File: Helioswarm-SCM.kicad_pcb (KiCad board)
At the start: 8 copper layers, 38 parts, among them U201 ASIC_JUICE

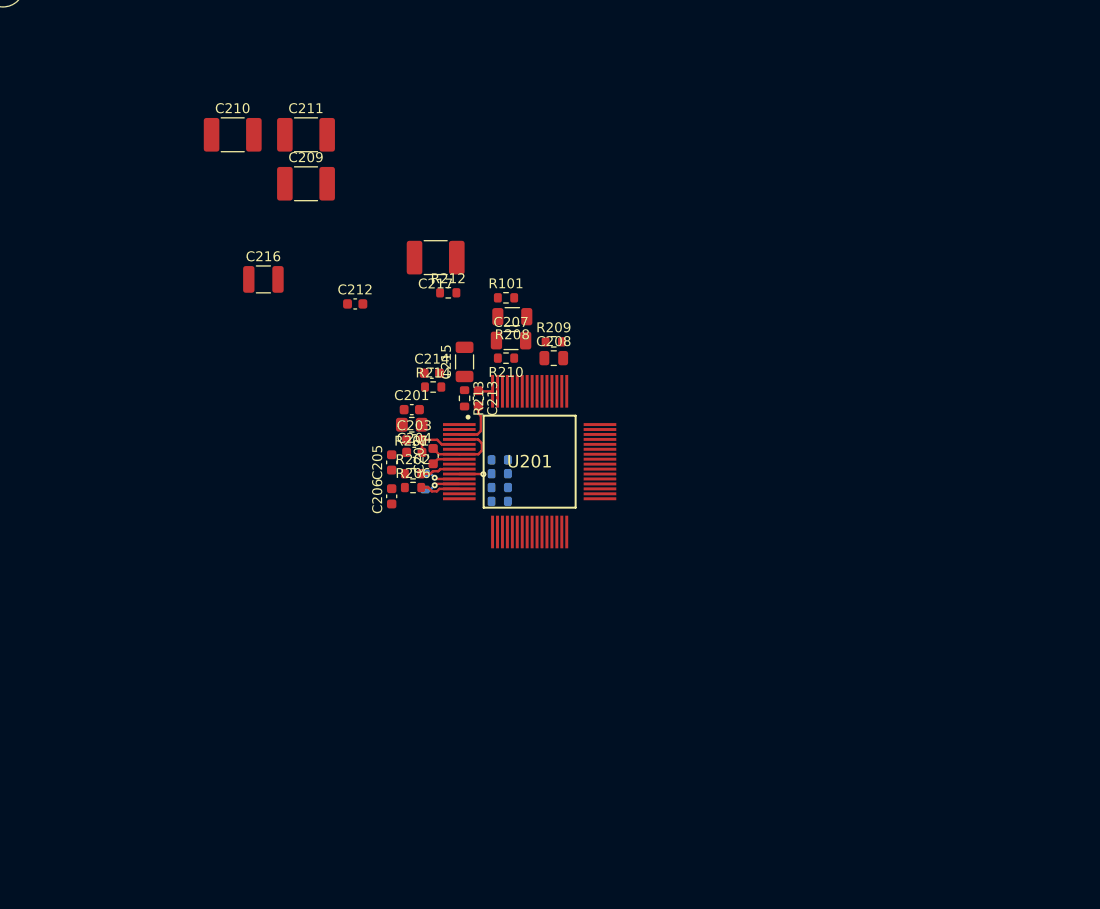
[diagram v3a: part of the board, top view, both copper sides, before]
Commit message: Layout WIP
Asic mostly routed, D-Sub connectors layout started.

Signed-off-by: Alexis Jeandet <alexis.jeandet@member.fsf.org>
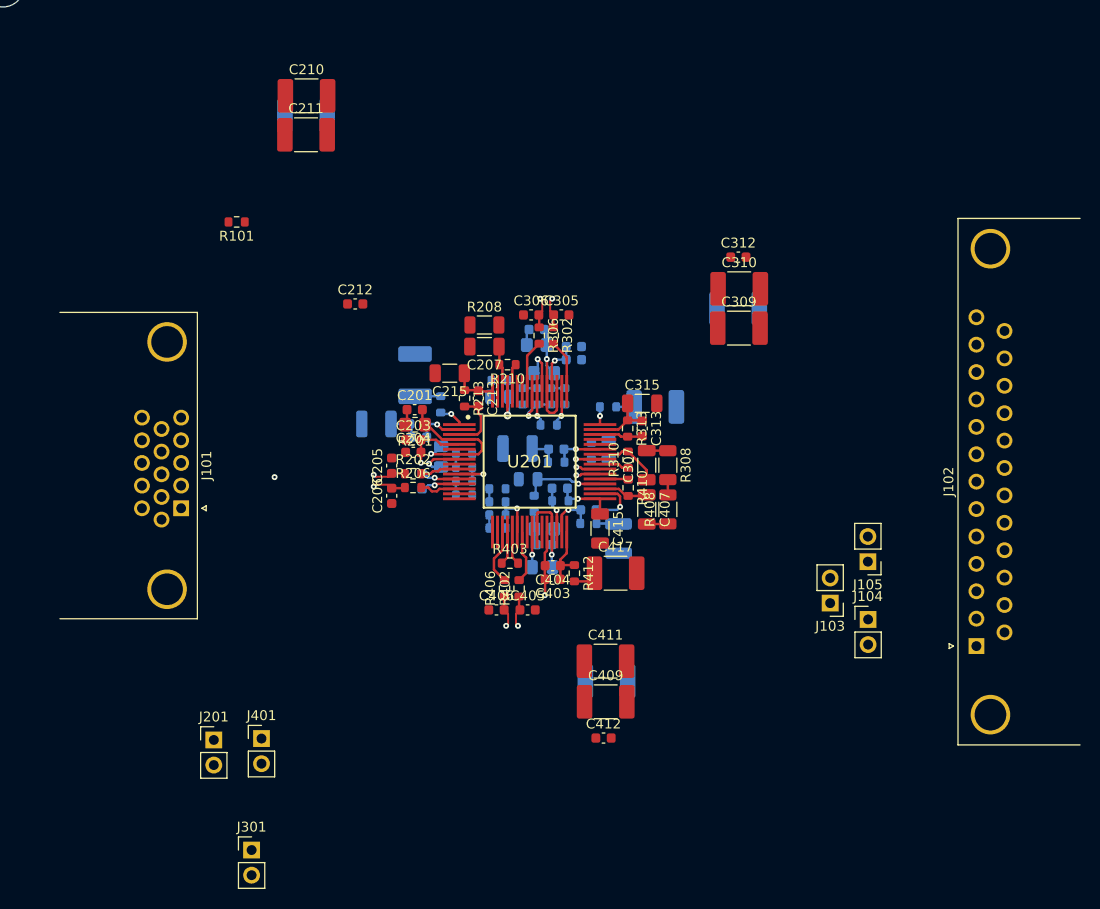
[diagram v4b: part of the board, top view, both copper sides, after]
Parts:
- added C301: *, Capacitor_SMD:C_0603_1608Metric, B.Cu at (156.3, 73.6)
- added C302: *, Capacitor_SMD:C_0805_2012Metric_Pad1.18x1.45mm_HandSolder, B.Cu at (157.0, 78.0)
- added C303: *, Capacitor_SMD:C_0603_1608Metric, B.Cu at (160.0, 76.6)
- added C304: *, Capacitor_SMD:C_0603_1608Metric, B.Cu at (160.0, 75.3)
- added C305: *, Capacitor_SMD:C_0603_1608Metric, F.Cu at (158.8, 72.1)
- added C306: *, Capacitor_SMD:C_0603_1608Metric, F.Cu at (155.7, 72.1)
- added C307: 220n, Capacitor_SMD:C_1206_3216Metric, F.Cu at (167.4, 87.3)
- added C308: *, Capacitor_SMD:C_0805_2012Metric, B.Cu at (163.5, 85.7)
- added C309: 680n, Capacitor_SMD:C_1812_4532Metric_Pad1.57x3.40mm_HandSolder, F.Cu at (176.7, 73.4)
- added C310: 680n, Capacitor_SMD:C_1812_4532Metric_Pad1.57x3.40mm_HandSolder, F.Cu at (176.7, 69.4)
- added C311: 680n, Capacitor_SMD:C_1812_4532Metric_Pad1.57x3.40mm_HandSolder, B.Cu at (176.6, 71.4)
- added C312: 1n, Capacitor_SMD:C_0603_1608Metric, F.Cu at (176.6, 66.2)
- added C313: 221p, Capacitor_SMD:C_0603_1608Metric, F.Cu at (166.9, 83.6)
- added C314: 221p, Capacitor_SMD:C_0603_1608Metric, B.Cu at (158.2, 85.6)
- added C315: 220n, Capacitor_SMD:C_1206_3216Metric, F.Cu at (166.9, 81.0)
- added C316: 470nF, Capacitor_SMD:C_1210_3225Metric, B.Cu at (154.3, 85.6)
- added C317: 470n, Capacitor_SMD:C_1812_4532Metric_Pad1.57x3.40mm_HandSolder, B.Cu at (168.2, 81.4)
- added C401: *, Capacitor_SMD:C_0603_1608Metric, B.Cu at (157.0, 95.3)
- added C402: *, Capacitor_SMD:C_0805_2012Metric_Pad1.18x1.45mm_HandSolder, B.Cu at (156.8, 97.6)
- added C403: *, Capacitor_SMD:C_0603_1608Metric, F.Cu at (157.9, 98.8)
- added C404: *, Capacitor_SMD:C_0603_1608Metric, F.Cu at (157.9, 97.4)
- added C405: *, Capacitor_SMD:C_0603_1608Metric, F.Cu at (155.3, 101.9)
- added C406: *, Capacitor_SMD:C_0603_1608Metric, F.Cu at (152.2, 101.9)
- added C407: 220n, Capacitor_SMD:C_1206_3216Metric, F.Cu at (167.4, 91.7)
- added C408: *, Capacitor_SMD:C_0805_2012Metric, B.Cu at (155.4, 88.7)
- added C409: 680n, Capacitor_SMD:C_1812_4532Metric_Pad1.57x3.40mm_HandSolder, F.Cu at (163.2, 111.2)
- added C410: 680n, Capacitor_SMD:C_1812_4532Metric_Pad1.57x3.40mm_HandSolder, B.Cu at (163.3, 109.1)
- added C411: 680n, Capacitor_SMD:C_1812_4532Metric_Pad1.57x3.40mm_HandSolder, F.Cu at (163.2, 107.1)
- added C412: 1n, Capacitor_SMD:C_0603_1608Metric, F.Cu at (163.0, 114.9)
- added C413: 221p, Capacitor_SMD:C_0603_1608Metric, B.Cu at (158.6, 89.6)
- added C414: 221p, Capacitor_SMD:C_0603_1608Metric, B.Cu at (161.5, 91.8)
- added C415: 220n, Capacitor_SMD:C_1206_3216Metric, F.Cu at (162.7, 93.7)
- added C416: 470nF, Capacitor_SMD:C_1210_3225Metric, B.Cu at (164.5, 94.7)
- added C417: 470n, Capacitor_SMD:C_1812_4532Metric_Pad1.57x3.40mm_HandSolder, F.Cu at (164.2, 98.2)
- added J101: DB15_Male_MountingHoles, Connector_Dsub:DSUB-15-HD_Female_Horizontal_P2.29x1.98mm_EdgePinOffset8.35mm_Housed_MountingHolesOffset10.89mm, F.Cu at (120.3, 91.6)
- added J102: DB25_Female_MountingHoles, Connector_Dsub:DSUB-25_Male_Horizontal_P2.77x2.84mm_EdgePinOffset7.70mm_Housed_MountingHolesOffset9.12mm, F.Cu at (200.7, 105.6)
- added J103: Conn_01x02, Connector_PinHeader_2.54mm:PinHeader_1x02_P2.54mm_Vertical, F.Cu at (185.9, 101.2)
- added J104: Conn_01x02, Connector_PinHeader_2.54mm:PinHeader_1x02_P2.54mm_Vertical, F.Cu at (189.8, 102.9)
- added J105: Conn_01x02, Connector_PinHeader_2.54mm:PinHeader_1x02_P2.54mm_Vertical, F.Cu at (189.7, 97.0)
- added J201: Conn_01x02, Connector_PinHeader_2.54mm:PinHeader_1x02_P2.54mm_Vertical, F.Cu at (123.6, 115.0)
- added J301: Conn_01x02, Connector_PinHeader_2.54mm:PinHeader_1x02_P2.54mm_Vertical, F.Cu at (127.4, 126.2)
- added J401: Conn_01x02, Connector_PinHeader_2.54mm:PinHeader_1x02_P2.54mm_Vertical, F.Cu at (128.4, 114.9)
- added R301: 150k, Resistor_SMD:R_0805_2012Metric_Pad1.20x1.40mm_HandSolder, B.Cu at (156.3, 75.1)
- added R302: 49,9, Resistor_SMD:R_0603_1608Metric, F.Cu at (157.9, 74.2)
- added R303: 7,68k, Resistor_SMD:R_0603_1608Metric, B.Cu at (157.5, 83.2)
- added R304: 49,9k, Resistor_SMD:R_0603_1608Metric, B.Cu at (159.1, 80.3)
- added R305: TBD, Resistor_SMD:R_0603_1608Metric, B.Cu at (157.7, 80.3)
- added R306: 49,9, Resistor_SMD:R_0603_1608Metric, F.Cu at (156.5, 74.2)
- added R307: TBD, Resistor_SMD:R_0603_1608Metric, B.Cu at (156.3, 80.3)
- added R308: 750k, Resistor_SMD:R_1206_3216Metric, F.Cu at (169.5, 87.3)
- added R309: 42,2k, Resistor_SMD:R_0603_1608Metric, B.Cu at (161.8, 85.9)
- added R310: 24,9k, Resistor_SMD:R_0603_1608Metric, F.Cu at (165.5, 86.7)
- added R311: 49,9k, Resistor_SMD:R_0603_1608Metric, B.Cu at (154.8, 80.3)
- added R312: 400, Resistor_SMD:R_0603_1608Metric, B.Cu at (163.5, 81.4)
- added R313: 22,1k, Resistor_SMD:R_0603_1608Metric, F.Cu at (165.5, 83.6)
- added R314: 44,2k, Resistor_SMD:R_0603_1608Metric, B.Cu at (158.2, 87.0)
- added R401: 150k, Resistor_SMD:R_0805_2012Metric_Pad1.20x1.40mm_HandSolder, B.Cu at (157.0, 93.7)
- added R402: 49,9, Resistor_SMD:R_0603_1608Metric, F.Cu at (154.5, 99.7)
- added R403: 7,68k, Resistor_SMD:R_0603_1608Metric, F.Cu at (153.6, 97.2)
- added R404: 49,9k, Resistor_SMD:R_0603_1608Metric, B.Cu at (152.3, 93.6)
- added R405: TBD, Resistor_SMD:R_0603_1608Metric, B.Cu at (152.3, 92.3)
- added R406: 49,9, Resistor_SMD:R_0603_1608Metric, F.Cu at (153.0, 99.7)
- added R407: TBD, Resistor_SMD:R_0603_1608Metric, B.Cu at (152.3, 91.0)
- added R408: 750k, Resistor_SMD:R_1206_3216Metric, F.Cu at (169.5, 91.7)
- added R409: 42,2k, Resistor_SMD:R_0603_1608Metric, B.Cu at (156.0, 91.2)
- added R410: 24,9k, Resistor_SMD:R_0603_1608Metric, F.Cu at (165.5, 89.6)
- added R411: 49,9k, Resistor_SMD:R_0603_1608Metric, B.Cu at (152.3, 89.7)
- added R412: 400, Resistor_SMD:R_0603_1608Metric, F.Cu at (160.1, 98.2)
- added R413: 22,1k, Resistor_SMD:R_0603_1608Metric, B.Cu at (158.6, 90.9)
- added R414: 44,2k, Resistor_SMD:R_0603_1608Metric, B.Cu at (161.5, 93.2)
- C202: footprint Capacitor_SMD:C_0603_1608Metric -> Capacitor_SMD:C_0805_2012Metric_Pad1.18x1.45mm_HandSolder; moved to B.Cu
- C208, C209, C214, C216, C217, R209, R212, R214: moved to B.Cu
- moved R101 28.3 mm to (125.9, 62.7), turned to 180 degrees
- moved C216 18.5 mm to (140.1, 83.1), turned to 180 degrees
- moved C217 12.1 mm to (144.0, 78.2), turned to 90 degrees
- moved R212 11.3 mm to (146.6, 81.1), turned to 90 degrees
- moved C210 8.44 mm to (133.0, 49.9)
- moved C209 6.91 mm to (132.9, 51.9)
- moved C208 6.74 mm to (152.5, 80.4), turned to 180 degrees
- moved R209 6.74 mm to (152.5, 78.7), turned to 180 degrees
- moved C214 6.58 mm to (144.4, 84.4)
- moved R211 6.02 mm to (148.9, 86.1), turned to 0 degrees
- moved R204 5.06 mm to (148.9, 90.3), turned to 0 degrees
- moved R207 4.14 mm to (148.9, 87.5), turned to 180 degrees
- moved R214 4.01 mm to (144.3, 83.1)
- moved R205 3.69 mm to (148.9, 88.9), turned to 180 degrees
- moved R208 2.94 mm to (151.0, 73.1), turned to 0 degrees
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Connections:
- C201 pad 1: /ASIC_X_Channel/CR -> /CR_X
- R201 pad 2: /ASIC_X_Channel/CR -> /CR_X
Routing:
- net /SX-: track 0.00 -> 76.5 mm, vias 0 -> 1
- net /SX+: track 0.00 -> 76.4 mm, vias 0 -> 1
- net /SY-: track 0.00 -> 71.0 mm, vias 0 -> 1
- net /SY+: track 0.00 -> 69.8 mm, vias 0 -> 1
- net /SZ-: track 0.00 -> 56.3 mm, vias 0 -> 1
- net /SZ+: track 0.00 -> 55.1 mm, vias 0 -> 1
- net /SCM_Z: track 0.00 -> 50.7 mm, vias 0 -> 2
- net /SCM_Y: track 0.00 -> 47.8 mm, vias 0 -> 1
- net /SCM_X: track 5.23 -> 32.4 mm, vias 0 -> 1
- net /ASIC_Y_Channel/In2P: track 0.00 -> 13.1 mm, vias 0 -> 1
- net /ASIC_Z_Channel/In2P: track 0.00 -> 11.6 mm, vias 0 -> 1
- net /ASIC_Z_Channel/VDD: track 0.00 -> 9.39 mm, vias 0 -> 1
- net Net-(C408-Pad1): track 0.00 -> 8.31 mm, vias 0 -> 1
- net /ASIC_X_Channel/In2P: track 8.51 -> 15.9 mm, vias 0 -> 1
- net Net-(C307-Pad1): track 0.00 -> 6.60 mm
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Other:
- copper layers 8 -> 4

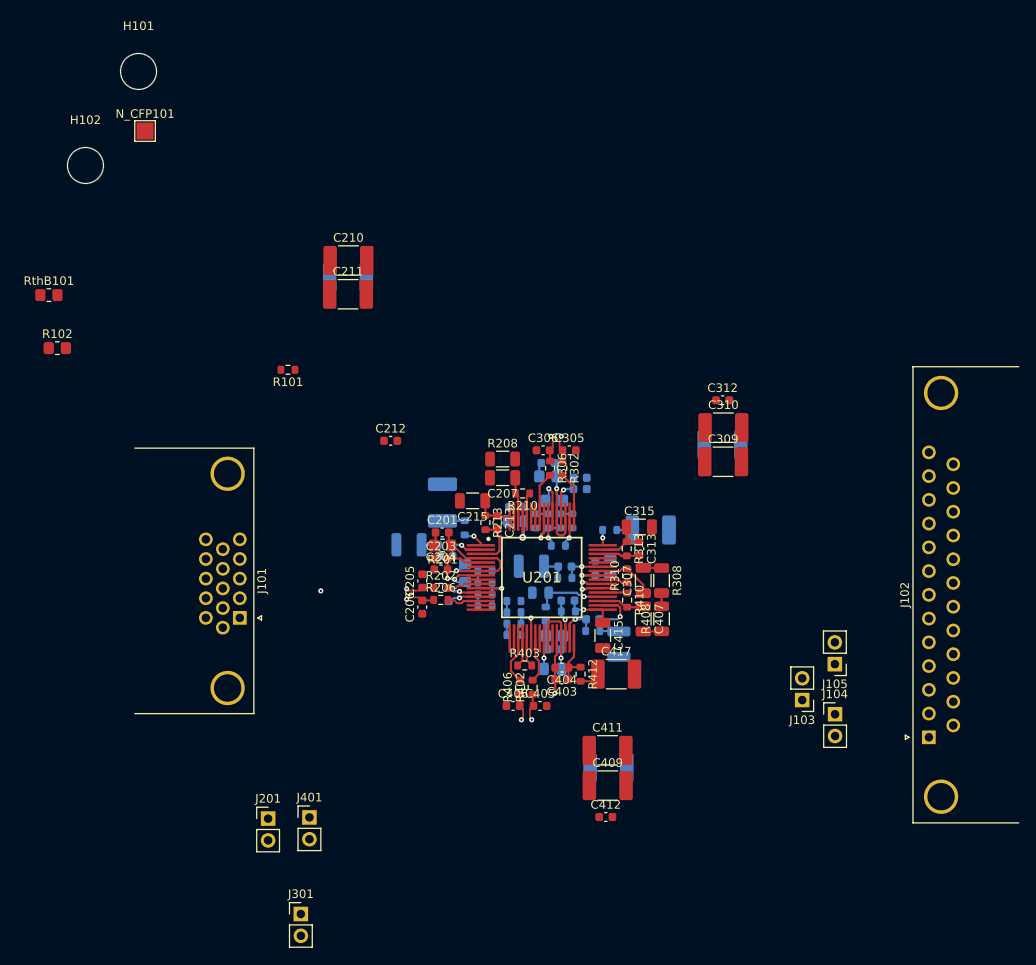
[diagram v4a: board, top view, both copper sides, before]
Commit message: PCB layout complete without silkscreen
Signed-off-by: Alexis Jeandet <alexis.jeandet@member.fsf.org>
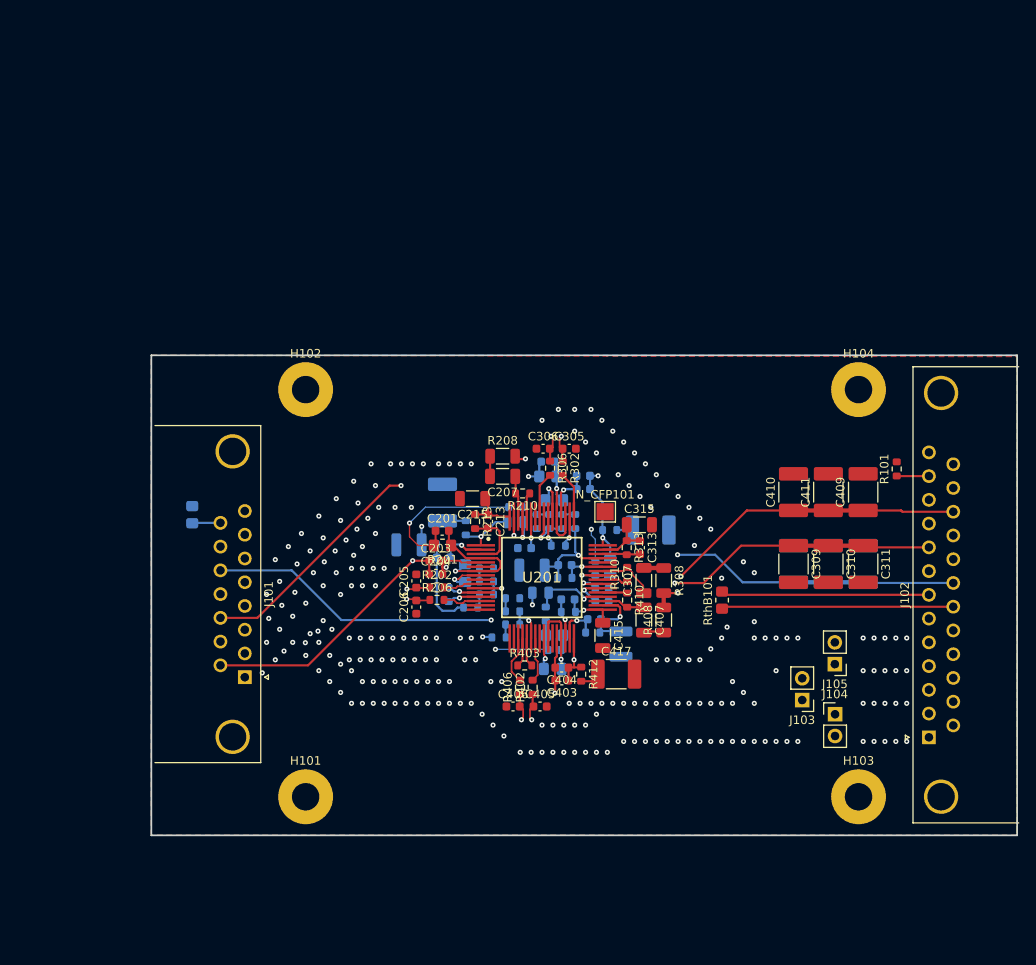
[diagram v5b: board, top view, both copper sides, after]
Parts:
- removed J201, J301, J401: Conn_01x02, Connector_PinHeader_2.54mm:PinHeader_1x02_P2.54mm_Vertical
- added H103: MountingHole_Pad, MountingHole:MountingHole_3.2mm_M3_Pad, F.Cu at (192.5, 112.5)
- added H104: MountingHole_Pad, MountingHole:MountingHole_3.2mm_M3_Pad, F.Cu at (192.5, 65.0)
- C210, C211, C212, C312, C412, R102: moved to B.Cu
- C311, C410: moved to F.Cu
- H101, H102: value MountingHole -> MountingHole_Pad; footprint LibPersoNadj:MountingHole_4.2 -> MountingHole:MountingHole_3.2mm_M3_Pad
- J101: value DB15_Male_MountingHoles -> DB15_Female_MountingHoles; footprint Connector_Dsub:DSUB-15-HD_Female_Horizontal_P2.29x1.98mm_EdgePinOffset8.35mm_Housed_MountingHolesOffset10.89mm -> Connector_Dsub:DSUB-15_Female_Horizontal_P2.77x2.84mm_EdgePinOffset7.70mm_Housed_MountingHolesOffset9.12mm
- moved H101 86.8 mm to (128.0, 112.5)
- moved RthB101 86.2 mm to (176.6, 89.6), turned to 90 degrees
- moved R101 72.0 mm to (197.0, 74.3), turned to 90 degrees
- moved C210 69.7 mm to (193.0, 85.3), turned to 90 degrees
- moved N_CFP101 69.7 mm to (162.9, 79.2)
- moved C211 64.3 mm to (189.0, 85.3), turned to 90 degrees
- moved C209 61.8 mm to (184.9, 85.3), turned to 90 degrees
- moved C409 45.4 mm to (193.0, 77.0), turned to 90 degrees
- moved C411 39.6 mm to (189.0, 77.0), turned to 90 degrees
- moved C410 38.7 mm to (184.9, 77.0), turned to 90 degrees
- moved H102 36.7 mm to (128.0, 65.0)
- moved C312 26.1 mm to (162.6, 88.2)
- moved C412 25.1 mm to (162.6, 89.7)
- moved R102 25.0 mm to (114.8, 79.6), turned to 90 degrees
- moved C311 21.5 mm to (193.0, 85.3), turned to 270 degrees
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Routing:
- net /SCM_TEMP_SENSOR_2: track 0.00 -> 117.0 mm
- net /SCM_TEMP_SENSOR_1: track 0.00 -> 116.5 mm
- net /CAL: track 1.55 -> 77.1 mm, vias 0 -> 2
- net /M_Y: track 1.79 -> 63.4 mm, vias 1 -> 3
- net /CR_Y: track 1.69 -> 58.4 mm, vias 0 -> 2
- net /VDD_X: track 0.00 -> 56.5 mm, vias 0 -> 2
- net /VDD_Z: track 2.44 -> 55.2 mm, vias 1 -> 2
- net /M_Z: track 6.48 -> 55.6 mm, vias 0 -> 3
- net /M_X: track 2.54 -> 46.8 mm, vias 1 -> 2
- net /VDD_Y: track 2.46 -> 46.1 mm, vias 1 -> 2
- net /CR_X: track 1.60 -> 44.3 mm, vias 0 -> 1
- net /CR_Z: track 3.39 -> 43.1 mm, vias 0 -> 2
- net /PCB_TEMP_SENSOR_1: track 0.00 -> 27.1 mm
- net /ASIC_X_Channel/VDD: track 3.33 -> 28.2 mm, vias 0 -> 2
- net /PCB_TEMP_SENSOR_2: track 0.00 -> 24.3 mm
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- added copper zone on B.Cu, net GND
- added copper zone on F.Cu, net GND
- added copper zone on In1.Cu, net GND
- added copper zone on In2.Cu, net GND
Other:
- board outline added: 101 x 56 mm

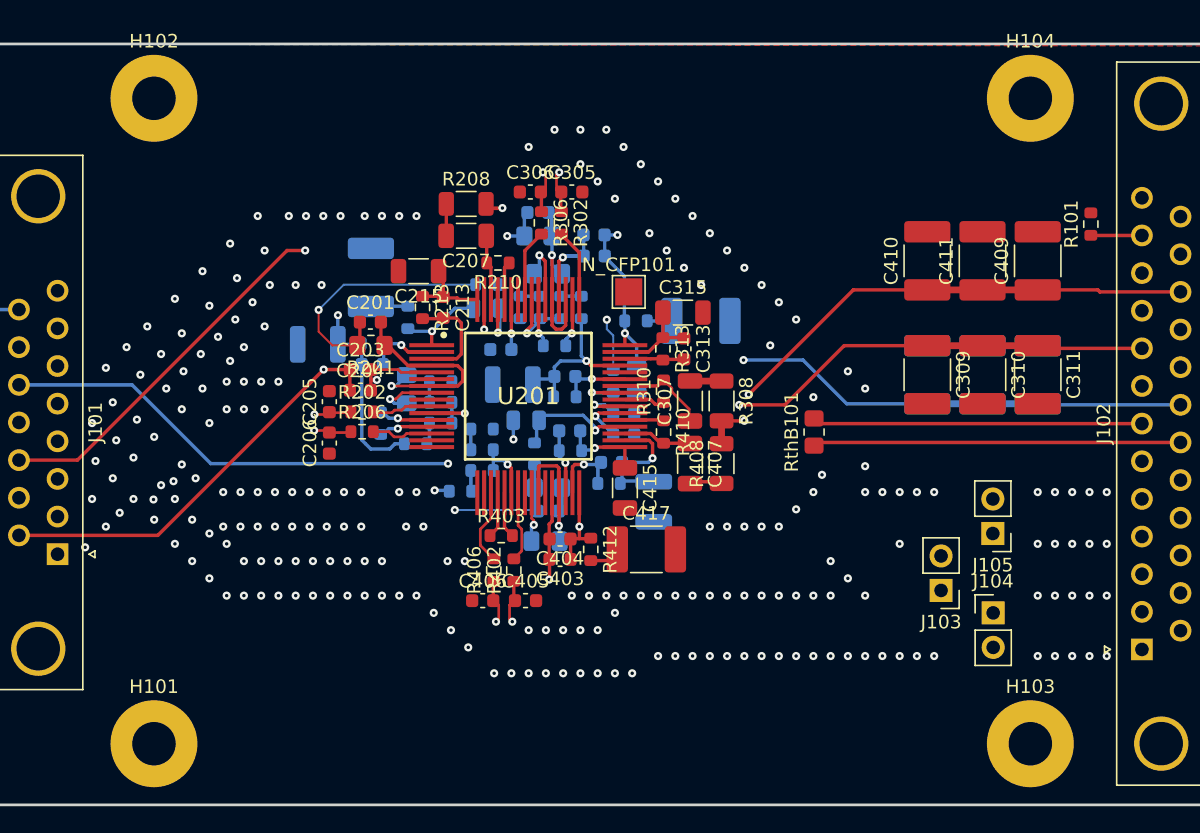
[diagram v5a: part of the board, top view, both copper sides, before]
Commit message: BBM PCB ready for review
Signed-off-by: Alexis Jeandet <alexis.jeandet@member.fsf.org>
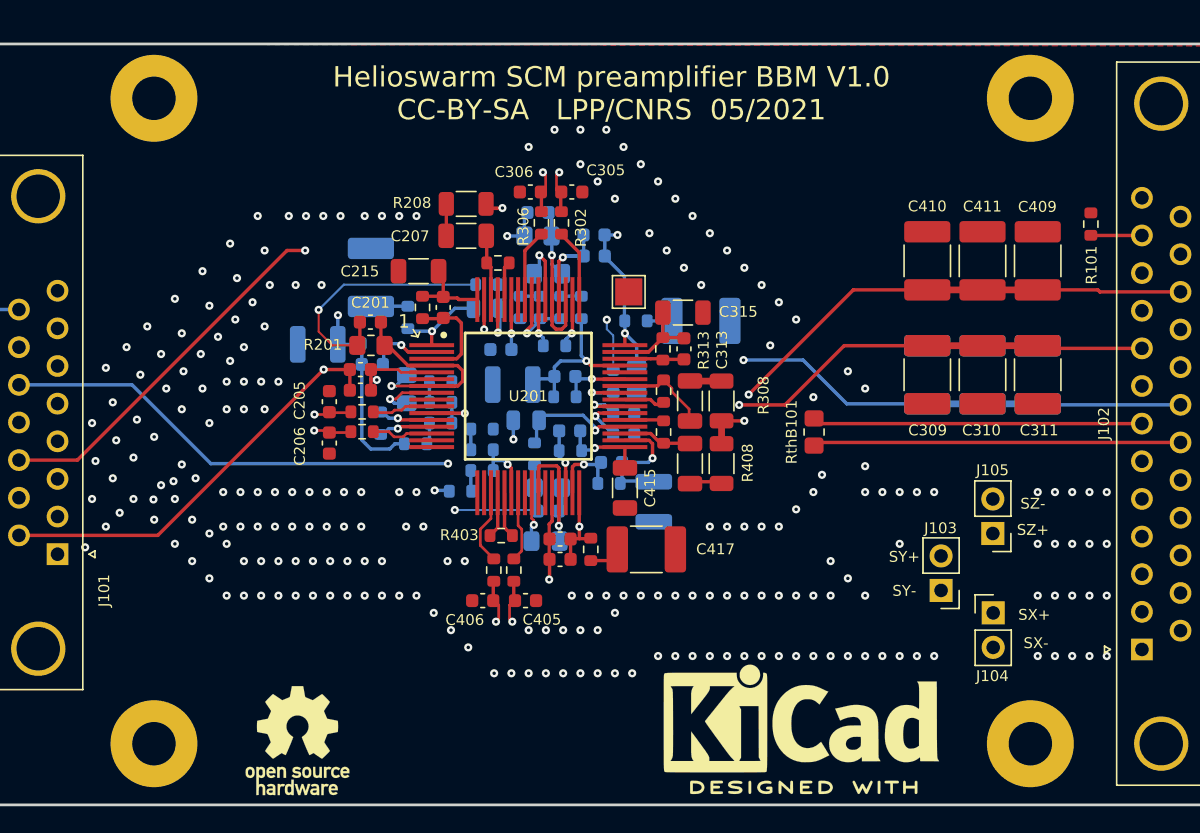
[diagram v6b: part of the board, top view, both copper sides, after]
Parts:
- added LOGO1: Logo_Open_Hardware_Small, Symbol:KiCad-Logo2_8mm_SilkScreen, F.Cu at (175.6, 110.6)
- added LOGO2: Logo_Open_Hardware_Small, Symbol:OSHW-Logo_7.5x8mm_SilkScreen, F.Cu at (138.6, 112.3)
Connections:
- J102 pad 11: (no net) -> /PWR_Shield_Z
- J102 pad 22: (no net) -> /PWR_Shield_Y
- J102 pad 25: (no net) -> /CAL_Shield
- J102 pad 8: (no net) -> /PWR_Shield_X
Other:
- board text added: "1"
- board text added: "Cal"
- board text added: "Helioswarm SCM preamplifier BBM V1.0 CC-BY-SA LPP/CNRS 05/2021"
- board text added: "MX"
- board text added: "MY"
- board text added: "MZ"
- board text added: "SX+"
- board text added: "SX-"
- board text added: "SY+"
- board text added: "SY-"
- board text added: "SZ+"
- board text added: "SZ-"
- board text added: "VDDX"
- board text added: "VDDY"
- board text added: "VDDZ"
